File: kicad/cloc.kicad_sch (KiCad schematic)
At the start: 87 parts, among them J1 Barrel_Jack_MountingPin, Q1 NMOS, Q2 NMOS, Q3 NMOS, U1 TPIC6B595, U10 TPIC6B595, U11 HDSP-7401, U12 HDSP-7401, U13 DS3231, U2 HDSP-7401, U3 TPIC6B595, U4 HDSP-7401, U5 TPIC6B595, U6 TPIC6B595, U7 HDSP-7401, U8 HDSP-7401, U9 TPIC6B595

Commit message: finish schematics
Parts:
- added BZ1: Buzzer, symbol Device:Buzzer
- added C15: 0.1u, symbol Device:C
- added D3, D4, D5, D6: LED, symbol Device:LED
- added R52, R53, R54, R55: 220, symbol Device:R
- added SW1, SW2: SW_Push, symbol Switch:SW_Push
- added SW3: RotaryEncoder_Switch, symbol Device:RotaryEncoder_Switch
- added U14: CD4094, symbol 4xxx:HEF4094B
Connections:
- net +3V3: now also C15.1, U14.16 (V_{DD})
- net +9V: now also U8.1 (CA), U8.6 (CA)
- net GND: now also BZ1.2 (-), C15.2, R52.2, R53.2, R54.2, R55.2, SW1.1, SW2.1, SW3.C, SW3.S2, U14.8 (V_{SS})
- net LED_PWM: now also A1.16 (GPIO12), U14.15 (OE); no longer A1.21 (GPIO16), U1.9 (~{G}), U10.9 (~{G}), U3.9 (~{G}), U5.9 (~{G}), U6.9 (~{G}), U9.9 (~{G})
- net at U13.3 (SCL): now also A1.2 (GPIO1); no longer A1.9 (GPIO6)
- net at U13.4 (SDA): now also A1.1 (GPIO0); no longer A1.10 (GPIO7)
- net at A1.11 (GPIO8): now also SW3.B
- net LED_DATA: now reaches A1.12 (GPIO9)
- net LED_DATA: now also U14.2 (D)
- net LED_CLK: now reaches A1.14 (GPIO10)
- net LED_CLK: now also U14.3 (CP)
- net LED_LATCH: now reaches A1.15 (GPIO11)
- net LED_LATCH: now also U14.1 (STR)
- net at A1.19 (GPIO14): now also SW1.2
- net at A1.20 (GPIO15): now also SW2.2
- net at A1.29 (GPIO22): now also BZ1.1 (+)
- new net: D4.1 (K), R53.1
- new net: D3.1 (K), R52.1
- new net: D3.2 (A), U14.4 (QP0)
- new net: D4.2 (A), U14.5 (QP1)
- new net: D5.2 (A), U14.6 (QP2)
- new net: D6.2 (A), U14.7 (QP3)
- new net: D5.1 (K), R54.1
- new net: D6.1 (K), R55.1
- new net: A1.10 (GPIO7), SW3.A
- new net: A1.9 (GPIO6), SW3.S1
- new net DISPLAY_PWM: A1.21 (GPIO16), U1.9 (~{G}), U10.9 (~{G}), U3.9 (~{G}), U5.9 (~{G}), U6.9 (~{G}), U9.9 (~{G})
- no-connect marks 4 -> 23
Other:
- note added: "Both buttons use the pico's internal pull-up resistors"
- moved on the sheet: A1, C1, C10, C11, C12, C13, C14, C2, C3, C4, C5, C6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

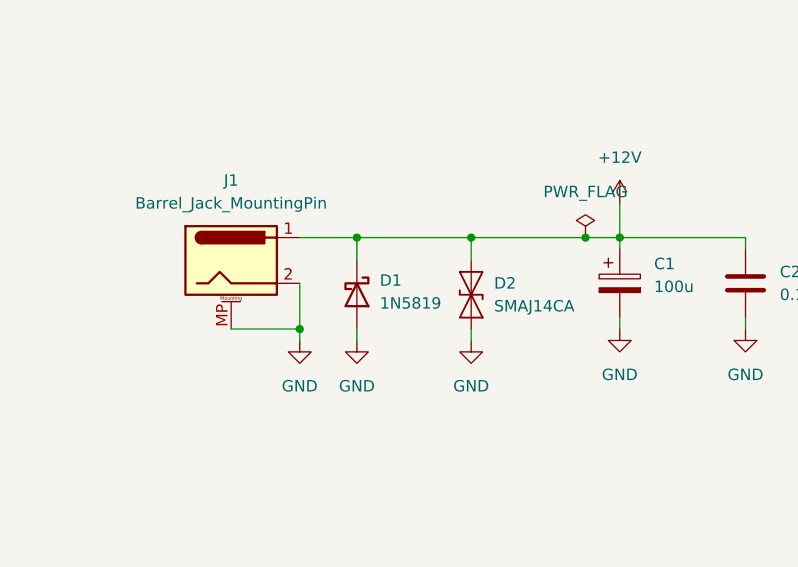
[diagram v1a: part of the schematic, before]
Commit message: fix ERC
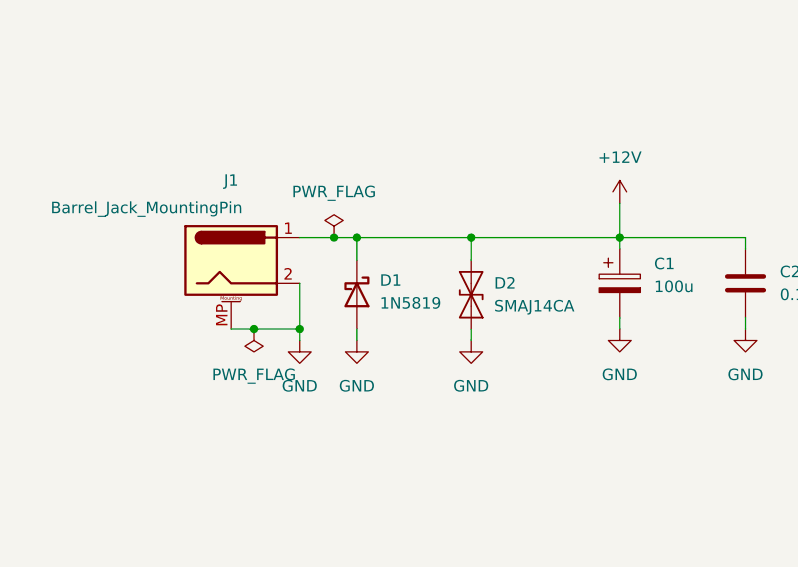
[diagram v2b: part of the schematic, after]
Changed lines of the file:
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@@
 	)
 	(junction
-		(at 78.74 44.45)
-		(diameter 0)
-		(color 0 0 0 0)
-	)
-	(junction
 		(at 266.7 170.18)
 		(diameter 0)
@@
 	)
 	(junction
+		(at 50.8 44.45)
+		(diameter 0)
+		(color 0 0 0 0)
+	)
+	(junction
 		(at 339.09 176.53)
 		(diameter 0)
@@
 	)
 	(junction
+		(at 41.91 54.61)
+		(diameter 0)
+		(color 0 0 0 0)
+	)
+	(junction
 		(at 60.96 187.96)
 		(diameter 0)
@@
 	(wire
 		(pts
-			(xy 86.36 219.71) (xy 88.9 219.71)
+			(xy 66.04 44.45) (xy 82.55 44.45)
 		)
 		(stroke
@@
 	(wire
 		(pts
-			(xy 82.55 44.45) (xy 78.74 44.45)
+			(xy 86.36 219.71) (xy 88.9 219.71)
 		)
 		(stroke
@@
 	(wire
 		(pts
+			(xy 41.91 54.61) (xy 46.99 54.61)
+		)
+		(stroke
+			(width 0)
+			(type default)
+		)
+	)
+	(wire
+		(pts
 			(xy 40.64 154.94) (xy 40.64 163.83)
 		)
@@
 	(wire
 		(pts
+			(xy 53.34 44.45) (xy 66.04 44.45)
+		)
+		(stroke
+			(width 0)
+			(type default)
+		)
+	)
+	(wire
+		(pts
 			(xy 67.31 149.86) (xy 44.45 149.86)
 		)
@@
 	(wire
 		(pts
-			(xy 53.34 44.45) (xy 66.04 44.45)
-		)
-		(stroke
-			(width 0)
-			(type default)
-		)
-	)
-	(wire
-		(pts
 			(xy 308.61 72.39) (xy 308.61 97.79)
 		)
@@
 	(wire
 		(pts
-			(xy 78.74 44.45) (xy 66.04 44.45)
+			(xy 22.86 157.48) (xy 22.86 163.83)
 		)
 		(stroke
@@
 	(wire
 		(pts
-			(xy 22.86 157.48) (xy 22.86 163.83)
+			(xy 50.8 44.45) (xy 53.34 44.45)
 		)
 		(stroke
@@
 	(wire
 		(pts
-			(xy 39.37 54.61) (xy 46.99 54.61)
+			(xy 39.37 54.61) (xy 41.91 54.61)
 		)
 		(stroke
@@
 	(wire
 		(pts
-			(xy 46.99 44.45) (xy 53.34 44.45)
+			(xy 46.99 44.45) (xy 50.8 44.45)
 		)
 		(stroke
@@
 	(symbol
 		(lib_id "power:PWR_FLAG")
-		(at 78.74 44.45 0)
+		(at 50.8 44.45 0)
 		(unit 1)
 		(exclude_from_sim no)
@@
 		(fields_autoplaced yes)
 		(property "Reference" "#FLG01"
-			(at 78.74 42.545 0)
+			(at 50.8 42.545 0)
 			(effects
 				(font
@@
 		)
 		(property "Value" "PWR_FLAG"
-			(at 78.74 39.37 0)
+			(at 50.8 39.37 0)
 			(effects
 				(font
@@
 		)
 		(property "Footprint" ""
-			(at 78.74 44.45 0)
+			(at 50.8 44.45 0)
 			(effects
 				(font
@@
 		)
 		(property "Datasheet" "~"
-			(at 78.74 44.45 0)
+			(at 50.8 44.45 0)
 			(effects
 				(font
@@
 		)
 		(property "Description" "Special symbol for telling ERC where power comes from"
-			(at 78.74 44.45 0)
+			(at 50.8 44.45 0)
 			(effects
 				(font
@@
 		(on_board yes)
 		(dnp no)
-		(fields_autoplaced yes)
 		(property "Reference" "J1"
 			(at 39.37 38.1 0)
@@
 		)
 		(property "Value" "Barrel_Jack_MountingPin"
-			(at 39.37 40.64 0)
+			(at 29.972 41.148 0)
 			(effects
 				(font
@@
 					(unit 1)
 				)
+			)
+		)
+	)
+	(symbol
+		(lib_id "power:PWR_FLAG")
+		(at 41.91 54.61 180)
+		(unit 1)
+		(exclude_from_sim no)
+		(in_bom yes)
+		(on_board yes)
+		(dnp no)
+		(fields_autoplaced yes)
+		(property "Reference" "#FLG02"
+			(at 41.91 56.515 0)
+			(effects
+				(font
+					(size 1.27 1.27)
+				)
+				(hide yes)
+			)
+		)
+		(property "Value" "PWR_FLAG"
+			(at 41.91 59.69 0)
+			(effects
+				(font
+					(size 1.27 1.27)
+				)
+			)
+		)
+		(property "Footprint" ""
+			(at 41.91 54.61 0)
+			(effects
+				(font
+					(size 1.27 1.27)
+				)
+				(hide yes)
+			)
+		)
+		(property "Datasheet" "~"
+			(at 41.91 54.61 0)
+			(effects
+				(font
+					(size 1.27 1.27)
+				)
+				(hide yes)
+			)
+		)
+		(property "Description" "Special symbol for telling ERC where power comes from"
+			(at 41.91 54.61 0)
+			(effects
+				(font
+					(size 1.27 1.27)
+				)
+				(hide yes)
+			)
+		)
+		(pin "1"
+		)
+		(instances
+			(project "cloc"
+				(path "/f597545d-e439-405e-b3d9-45b4756804a9"
+					(reference "#FLG02")
+					(unit 1)
+				)

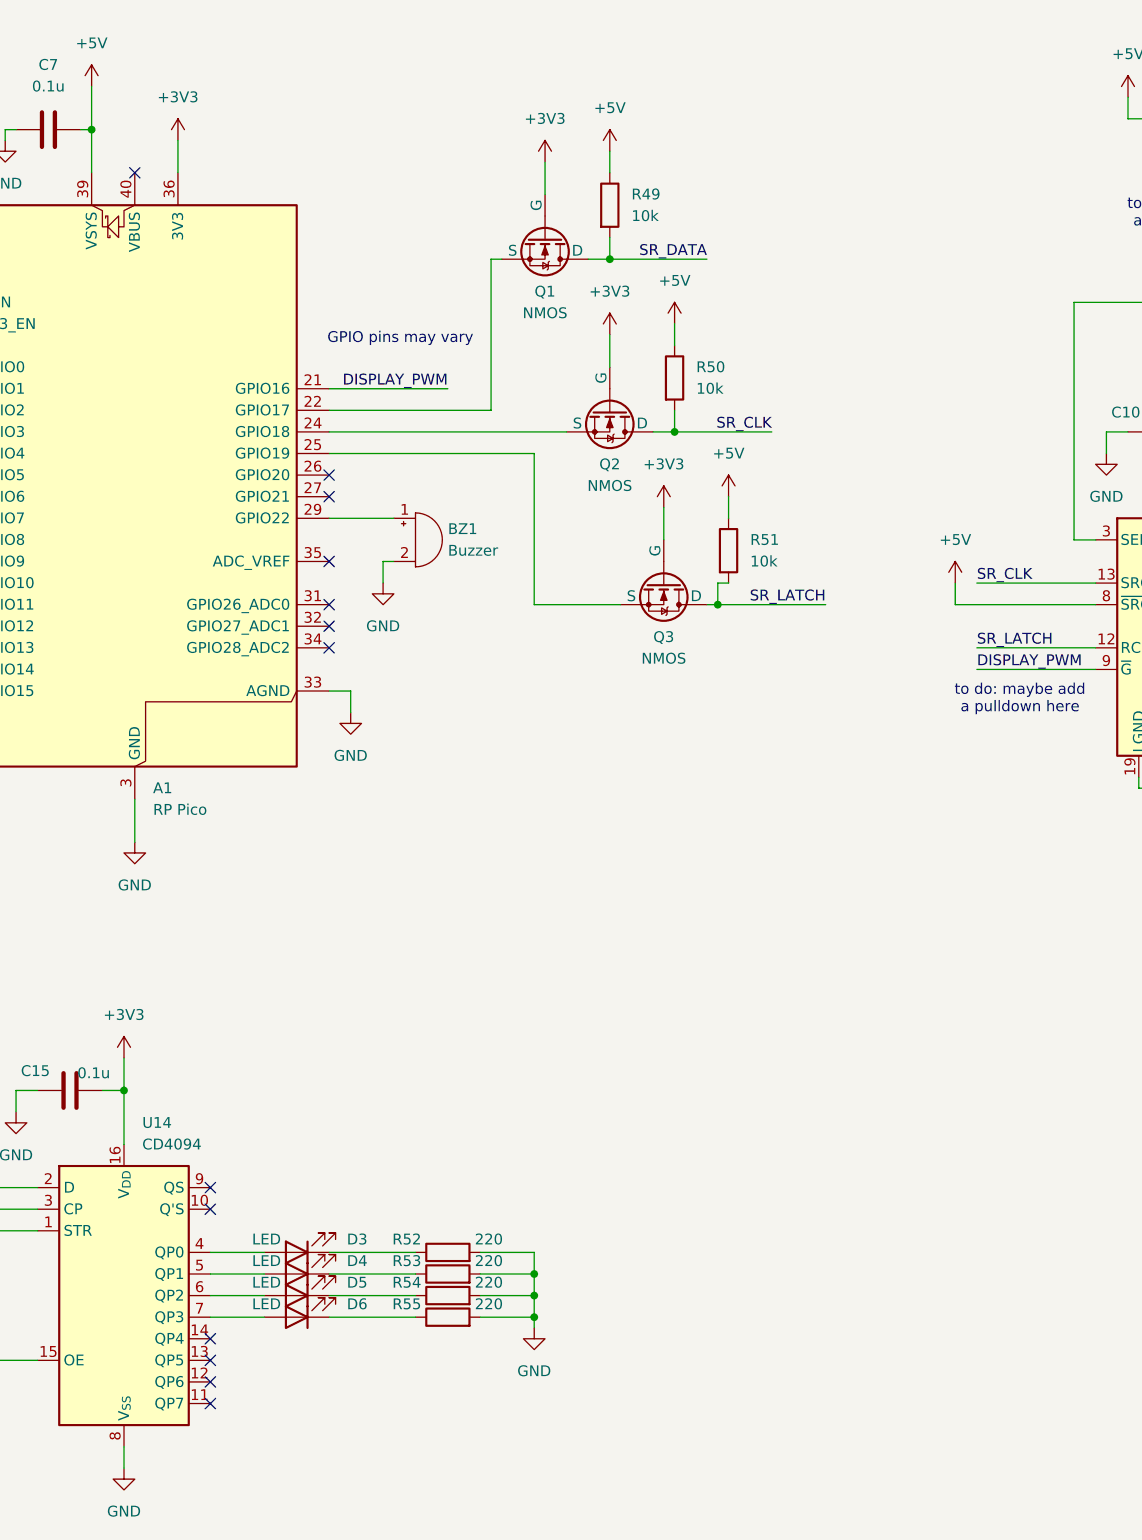
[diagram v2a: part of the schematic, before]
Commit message: add screen to schematics
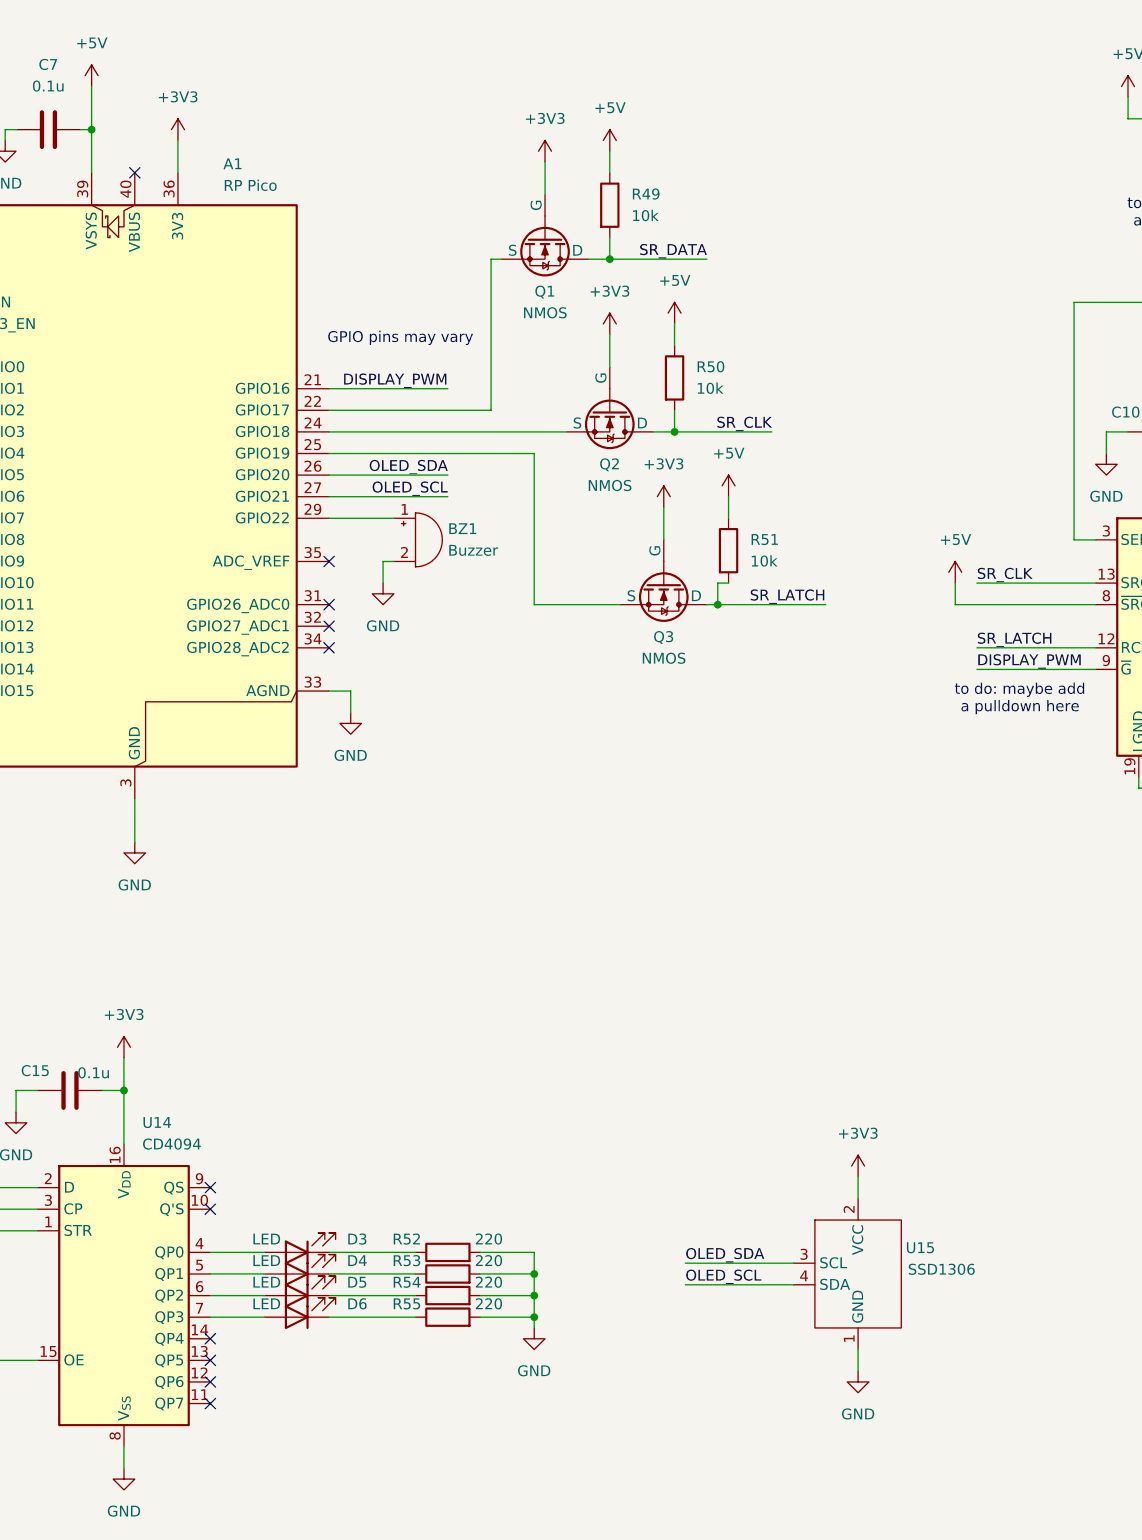
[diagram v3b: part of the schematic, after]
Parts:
- added U15: SSD1306, symbol Display_Graphic:SSD1306
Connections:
- net +3V3: now also U15.2 (VCC)
- net GND: now also U15.1 (GND)
- net OLED_SDA: now reaches A1.26 (GPIO20)
- net OLED_SDA: now also U15.3 (SCL)
- net OLED_SCL: now reaches A1.27 (GPIO21)
- net OLED_SCL: now also U15.4 (SDA)
- no-connect marks 23 -> 21
